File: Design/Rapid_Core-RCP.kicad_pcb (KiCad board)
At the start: 4 copper layers, 222 parts, among them IC1 TLIN1039DDFRQ1, IC2 TLIN1039DDFRQ1, IC3 SHT30A-DIS-B2.5KS, IC4 LM60440ARPKR, J1 CMD PIN, J10 CAN-1, J11 RS-485_1, J12 RS-485_2, J14 CAN-2, J15 Input Power, J2 CMD PIN, J3 LIN_1, J4 LIN_2, J5 GPIO_CONN_x_4, J6 SWD_Debug, J7 SPI_CONN, J8 USART, SW1 SW_Push, U1 STM32F446RETx, U2 ISO1042BQDWVRQ1, U3 ISO3082DW, U4 ISO3082DW, U5 ISO1042BQDWVRQ1, U6 CRE1S0505S3C, U7 CRE1S0505S3C, U8 LP3963-3.3, Y1 8_MHz, Y2 32.768_KHz

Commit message: PCB design started, comps arranged
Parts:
- removed FB1: FerriteBead, Inductor_SMD:L_0805_2012Metric_Pad1.05x1.20mm_HandSolder
- removed R11, R12, R13, R14: 0, Resistor_SMD:R_0603_1608Metric_Pad0.98x0.95mm_HandSolder
- J7: value SPI_CONN -> SPI; footprint Connector_PinHeader_2.54mm:PinHeader_1x10_P2.54mm_Vertical -> Connector_PinHeader_2.54mm:PinHeader_1x05_P2.54mm_Vertical
- L1, L2, L3: value 51uH 0.2A 1R -> ACT45B-510-2P-TL003
- L4: value 51u 0.2A 1R -> ACT45B-510-2P-TL003
- TP1, TP10, TP11, TP12, TP13, TP14, TP15, TP16, TP17, TP18, TP19, TP2, TP20, TP21, TP22, TP23, TP24, TP25, TP26, TP27, TP28, TP29, TP3, TP30, TP31, TP32, TP33, TP34, TP35, TP36, TP37, TP38, TP39, TP4, TP40, TP41, TP42, TP43, TP44, TP45, TP46, TP47, TP48, TP49, TP5, TP50, TP51, TP52, TP53, TP54, TP55, TP56, TP57, TP58, TP59, TP6, TP60, TP61, TP62, TP7, TP8, TP9: footprint TestPoint:TestPoint_Pad_D2.5mm -> TestPoint:TestPoint_Pad_D1.0mm
- moved TP10 218.4 mm to (-42.5, 142.7)
- moved TP3 218.4 mm to (-47.1, 133.6)
- moved TP4 218.4 mm to (-47.1, 138.1)
- moved TP5 218.4 mm to (-47.1, 142.7)
- moved TP6 218.4 mm to (-42.5, 124.5)
- moved TP7 218.4 mm to (-42.5, 129.0)
- moved TP8 218.4 mm to (-42.5, 133.6)
- moved TP9 218.4 mm to (-42.5, 138.1)
- moved C62 218.4 mm to (-66.9, 87.7)
- moved TP11 218.4 mm to (-38.0, 124.5)
- moved TP12 218.4 mm to (-38.0, 129.0)
- moved TP13 218.4 mm to (-38.0, 133.6)
- moved TP14 218.4 mm to (-38.0, 138.1)
- moved TP45 215.6 mm to (305.0, 155.4)
- moved TP46 215.6 mm to (305.0, 160.0)
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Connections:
- net /Communication_interface/CAN1_RX_R renamed /Communication_interface/CAN1_RX_R-1
- net /Communication_interface/CAN1_TX_R renamed /Communication_interface/CAN1_TX_R-1
- net /Communication_interface/CAN2_RX_R renamed /Communication_interface/CAN2_RX_R-2
- net /Communication_interface/CAN2_TX_R renamed /Communication_interface/CAN2_TX_R-2
- net /Communication_interface/RS-485_1_EN_R renamed /Communication_interface/RS-485_1_EN_R-1
- net /Communication_interface/RS-485_1_RX_R renamed /Communication_interface/RS-485_1_RX_R-1
- net /Communication_interface/RS-485_1_TX_R renamed /Communication_interface/RS-485_1_TX_R-1
- net /Communication_interface/RS-485_2_EN_R renamed /Communication_interface/RS-485_2_EN_R-2
- net /Communication_interface/RS-485_2_RX_R renamed /Communication_interface/RS-485_2_RX_R-2
- net /Communication_interface/RS-485_2_TX_R renamed /Communication_interface/RS-485_2_TX_R-2
- C15 pad 1: /FIL_FB -> +3.3V
- C18 pad 1: /FIL_FB -> +3.3V
- D5 pad 1: /Communication_interface/CAN_H -> /Communication_interface/CAN_H_IN-1
- D5 pad 2: /Communication_interface/CAN_L -> /Communication_interface/CAN_L_IN-1
- D6 pad 1: /Communication_interface/RS-485_B -> /Communication_interface/RS-485_B_IN-2
- D6 pad 2: /Communication_interface/RS-485_A -> /Communication_interface/RS-485_A_IN-2
- D7 pad 1: /Communication_interface/RS-485_B -> /Communication_interface/RS-485_B_IN-1
- D7 pad 2: /Communication_interface/RS-485_A -> /Communication_interface/RS-485_A-IN-1
- D8 pad 1: /Communication_interface/CAN_H -> /Communication_interface/CAN_H_IN-2
- D8 pad 2: /Communication_interface/CAN_L -> /Communication_interface/CAN_L_IN-2
- J10 pad 1: /Communication_interface/CAN_H -> /Communication_interface/CAN_L_IN-1
- J10 pad 2: /Communication_interface/CAN_L -> /Communication_interface/CAN_H_IN-1
- J11 pad 1: /Communication_interface/RS-485_B -> /Communication_interface/RS-485_A-IN-1
- J11 pad 2: /Communication_interface/RS-485_A -> /Communication_interface/RS-485_B_IN-1
- J12 pad 1: /Communication_interface/RS-485_B -> /Communication_interface/RS-485_A_IN-2
- J12 pad 2: /Communication_interface/RS-485_A -> /Communication_interface/RS-485_B_IN-2
- J14 pad 1: /Communication_interface/CAN_H -> /Communication_interface/CAN_L_IN-2
- J14 pad 2: /Communication_interface/CAN_L -> /Communication_interface/CAN_H_IN-2
- J15 pad 1: GND1 -> +24V
- J15 pad 2: +24V -> GND1
- L1 pad 1: /Communication_interface/CAN_H -> /Communication_interface/CAN_H-1
- L1 pad 2: /Communication_interface/CAN_H -> /Communication_interface/CAN_L-1
- L1 pad 3: /Communication_interface/CAN_L -> /Communication_interface/CAN_L_IN-1
- L1 pad 4: /Communication_interface/CAN_L -> /Communication_interface/CAN_H_IN-1
- L2 pad 1: /Communication_interface/RS-485_B -> /Communication_interface/RS-485_B-1
- L2 pad 2: /Communication_interface/RS-485_B -> /Communication_interface/RS-485_A-1
- L2 pad 3: /Communication_interface/RS-485_A -> /Communication_interface/RS-485_A-IN-1
- L2 pad 4: /Communication_interface/RS-485_A -> /Communication_interface/RS-485_B_IN-1
- L3 pad 1: /Communication_interface/RS-485_B -> /Communication_interface/RS-485_B-2
- L3 pad 2: /Communication_interface/RS-485_B -> /Communication_interface/RS-485_A-2
- L3 pad 3: /Communication_interface/RS-485_A -> /Communication_interface/RS-485_A_IN-2
- L3 pad 4: /Communication_interface/RS-485_A -> /Communication_interface/RS-485_B_IN-2
- L4 pad 1: /Communication_interface/CAN_H -> /Communication_interface/CAN_H-2
- L4 pad 2: /Communication_interface/CAN_H -> /Communication_interface/CAN_L-2
- L4 pad 3: /Communication_interface/CAN_L -> /Communication_interface/CAN_L_IN-2
- L4 pad 4: /Communication_interface/CAN_L -> /Communication_interface/CAN_H_IN-2
- R23 pad 1: /Communication_interface/CAN_H -> /Communication_interface/CAN_H-1
- R23 pad 2: /Communication_interface/CAN_H -> /Communication_interface/CAN_H_IN-1
- R24 pad 1: /Communication_interface/CAN_L -> /Communication_interface/CAN_L-1
- R24 pad 2: /Communication_interface/CAN_L -> /Communication_interface/CAN_L_IN-1
- R25 pad 1: /Communication_interface/RS-485_B -> /Communication_interface/RS-485_B-1
- R25 pad 2: /Communication_interface/RS-485_B -> /Communication_interface/RS-485_B_IN-1
- R26 pad 1: /Communication_interface/RS-485_A -> /Communication_interface/RS-485_A-1
- R26 pad 2: /Communication_interface/RS-485_A -> /Communication_interface/RS-485_A-IN-1
- R27 pad 1: /Communication_interface/CAN_H -> /Communication_interface/CAN_H_IN-1
- R27 pad 2: /Communication_interface/CAN_L -> /Communication_interface/CAN_L_IN-1
- R28 pad 1: /Communication_interface/RS-485_A -> /Communication_interface/RS-485_A-2
- R28 pad 2: /Communication_interface/RS-485_A -> /Communication_interface/RS-485_A_IN-2
- R29 pad 1: /Communication_interface/RS-485_B -> /Communication_interface/RS-485_B-2
- R29 pad 2: /Communication_interface/RS-485_B -> /Communication_interface/RS-485_B_IN-2
- R30 pad 1: /Communication_interface/RS-485_B -> /Communication_interface/RS-485_B-2
- R31 pad 1: /Communication_interface/RS-485_A -> /Communication_interface/RS-485_A-2
- R32 pad 1: /Communication_interface/RS-485_B -> /Communication_interface/RS-485_B-1
- R33 pad 1: /Communication_interface/RS-485_A -> /Communication_interface/RS-485_A-1
- R34 pad 1: /Communication_interface/RS-485_B -> /Communication_interface/RS-485_B_IN-2
- R34 pad 2: /Communication_interface/RS-485_A -> /Communication_interface/RS-485_A_IN-2
- R35 pad 1: /Communication_interface/RS-485_B -> /Communication_interface/RS-485_B_IN-1
- R35 pad 2: /Communication_interface/RS-485_A -> /Communication_interface/RS-485_A-IN-1
- R38 pad 1: /Communication_interface/CAN_H -> /Communication_interface/CAN_H-2
- R38 pad 2: /Communication_interface/CAN_H -> /Communication_interface/CAN_H_IN-2
- R39 pad 1: /Communication_interface/CAN_L -> /Communication_interface/CAN_L-2
- R39 pad 2: /Communication_interface/CAN_L -> /Communication_interface/CAN_L_IN-2
- R40 pad 1: /Communication_interface/CAN_H -> /Communication_interface/CAN_H_IN-2
- R40 pad 2: /Communication_interface/CAN_L -> /Communication_interface/CAN_L_IN-2
- R47 pad 1: /Communication_interface/CAN_H -> /Communication_interface/CAN_H_IN-1
- R48 pad 2: /Communication_interface/CAN_L -> /Communication_interface/CAN_L_IN-1
- TP43 pad 1: /Communication_interface/CAN_H -> /Communication_interface/CAN_H_IN-1
- TP44 pad 1: /Communication_interface/CAN_L -> /Communication_interface/CAN_L_IN-1
- TP45 pad 1: /Communication_interface/RS-485_A -> /Communication_interface/RS-485_A_IN-2
- TP46 pad 1: /Communication_interface/RS-485_B -> /Communication_interface/RS-485_B_IN-2
- TP47 pad 1: /Communication_interface/RS-485_B -> /Communication_interface/RS-485_B_IN-1
- TP48 pad 1: /Communication_interface/RS-485_A -> /Communication_interface/RS-485_A-IN-1
- TP51 pad 1: /Communication_interface/CAN_H -> /Communication_interface/CAN_H_IN-2
- TP52 pad 1: /Communication_interface/CAN_L -> /Communication_interface/CAN_L_IN-2
- U1 pad 10: /SPI2_MISO -> unconnected-(U1-PC2-Pad10)
- U1 pad 9: /SPI2_MOSI -> unconnected-(U1-PC1-Pad9)
- U2 pad 6: /Communication_interface/CAN_L -> /Communication_interface/CAN_L-1
- U2 pad 7: /Communication_interface/CAN_H -> /Communication_interface/CAN_H-1
- U3 pad 12: /Communication_interface/RS-485_A -> /Communication_interface/RS-485_A-1
- U3 pad 13: /Communication_interface/RS-485_B -> /Communication_interface/RS-485_B-1
- U4 pad 12: /Communication_interface/RS-485_A -> /Communication_interface/RS-485_A-2
- U4 pad 13: /Communication_interface/RS-485_B -> /Communication_interface/RS-485_B-2
- U5 pad 6: /Communication_interface/CAN_L -> /Communication_interface/CAN_L-2
- U5 pad 7: /Communication_interface/CAN_H -> /Communication_interface/CAN_H-2
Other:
- board outline added: 151.1 x 100.3 mm

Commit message: Temp complete of communication section , added Safety caps
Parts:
- removed C62: 4700pF, Capacitor_SMD:C_0603_1608Metric_Pad1.08x0.95mm_HandSolder
- removed R47, R48: 59, Resistor_SMD:R_0603_1608Metric_Pad0.98x0.95mm_HandSolder
- removed TP10, TP11, TP12, TP13, TP14, TP15, TP16, TP17, TP18, TP19, TP20, TP21, TP22, TP23, TP24, TP25, TP26, TP27, TP28, TP29, TP3, TP30, TP31, TP32, TP33, TP34, TP35, TP36, TP37, TP38, TP39, TP4, TP40, TP41, TP42, TP43, TP44, TP45, TP46, TP47, TP48, TP49, TP5, TP50, TP51, TP52, TP53, TP54, TP55, TP56, TP57, TP58, TP59, TP6, TP60, TP61, TP62, TP7, TP8, TP9: TestPoint, TestPoint:TestPoint_Pad_D1.0mm
- R15, R16, R17, R18, R19, R20, R21, R22, R23, R24, R25, R26, R28, R29, R36, R37, R38, R39: footprint Resistor_SMD:R_0603_1608Metric_Pad0.98x0.95mm_HandSolder -> Resistor_SMD:R_0805_2012Metric_Pad1.20x1.40mm_HandSolder
- R27, R34, R35, R40: footprint Resistor_SMD:R_0805_2012Metric_Pad1.20x1.40mm_HandSolder -> Resistor_SMD:R_2512_6332Metric_Pad1.40x3.35mm_HandSolder
- Y1: value 8_MHz -> Crystal_GND24; footprint ECS-2520MVLC_8MHz:ECS2520MVLC080BNTR -> Crystal:Crystal_SMD_2520-4Pin_2.5x2.0mm
- moved H3 126.5 mm to (213.6, 52.8)
- moved H4 94.5 mm to (213.4, 121.7)
- moved H1 88.8 mm to (76.5, 51.8)
- moved C16 78.1 mm to (121.7, 88.9), turned to 180 degrees
- moved C2 69.0 mm to (103.5, 79.7)
- moved C1 69.0 mm to (103.7, 77.9)
- moved R3 69.0 mm to (108.8, 84.0)
- moved R4 69.0 mm to (108.8, 81.0)
- moved IC3 69.0 mm to (104.0, 82.3)
- moved R20 67.8 mm to (154.1, 101.6)
- moved R22 67.7 mm to (154.1, 99.3)
- moved C31 67.6 mm to (158.2, 93.7)
- moved R21 67.5 mm to (154.1, 97.3)
- moved C29 67.3 mm to (160.3, 94.0)
- moved C27 67.0 mm to (162.1, 94.0)
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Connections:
- H3 pad 1: GND1 -> GND2
- H4 pad 1: GND1 -> GND2
- U1 pad 1: GND1 -> +3.3V
- U1 pad 29: /SPI2_SCK -> unconnected-(U1-PB10-Pad29)
- Y1 pad 1: GND1 -> /HSE_OUT
- Y1 pad 2: /HSE_IN -> GND1
- Y1 pad 3: /HSE_OUT -> /HSE_IN
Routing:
- net GND1: track 0.00 -> 79.4 mm, vias 0 -> 28
- net GND2: track 0.00 -> 63.8 mm, vias 0 -> 112
- net CAN1_TX: track 0.00 -> 38.4 mm
- net CAN1_RX: track 0.00 -> 38.1 mm
- net RS-485_1_RX: track 0.00 -> 27.6 mm
- net /Communication_interface/CAN_L_IN-2: track 0.00 -> 26.0 mm
- net /Communication_interface/CAN_H_IN-2: track 0.00 -> 25.1 mm
- net RS-485_1_EN: track 0.00 -> 24.7 mm, vias 0 -> 2
- net /Communication_interface/RS-485_A_IN-2: track 0.00 -> 24.6 mm
- net /Communication_interface/CAN_L_IN-1: track 0.00 -> 24.4 mm
- net /Communication_interface/CAN_H_IN-1: track 0.00 -> 24.0 mm
- net /Communication_interface/RS-485_B_IN-2: track 0.00 -> 24.0 mm
- net /Communication_interface/RS-485_A-IN-1: track 0.00 -> 23.5 mm
- net /Communication_interface/RS-485_B_IN-1: track 0.00 -> 23.3 mm
- net /HSE_OUT: track 0.00 -> 22.9 mm
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- added copper zone on F.Cu, net +3.3V
- added copper zone on B.Cu, net +5VA
- added copper zone on F.Cu, net +5VA
- added copper zone on F.Cu, net GND1
- added copper zone on In1.Cu, net GND2
- added copper zone on In2.Cu, net GND2
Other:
- board size 151.1 x 100.3 mm -> 144.3 x 77.7 mm
- rule pad_to_mask_clearance: 0 -> 0.08
- board text added: "Isolation _1"
- board text added: "Isolation _2"

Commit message: Added all the sections
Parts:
- removed FID4: Fiducial, Fiducial:Fiducial_1.5mm_Mask3mm
- R3, R4: value 10K -> 4k7
- moved FID3 131.4 mm to (205.7, 57.1)
- moved FID2 59.3 mm to (83.1, 53.3)
- moved C60 27.7 mm to (97.8, 56.6)
- moved R7 26.7 mm to (95.9, 84.8)
- moved D3 26.7 mm to (91.6, 84.8)
- moved C58 23.8 mm to (97.6, 58.9), turned to 0 degrees
- moved C59 23.7 mm to (93.5, 58.9), turned to 180 degrees
- moved R8 21.2 mm to (95.9, 82.3)
- moved D4 21.1 mm to (91.6, 82.3)
- moved L5 13.7 mm to (95.6, 63.8), turned to 90 degrees
- moved R41 13.3 mm to (84.9, 103.9)
- moved C57 11.9 mm to (100.9, 75.6)
- moved D2 11.2 mm to (122.7, 58.4)
- moved R46 11.2 mm to (97.3, 75.2), turned to 90 degrees
- moved R44 11.1 mm to (101.9, 71.3), turned to 0 degrees
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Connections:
- net /Power_Stage/LM_SW_1 renamed /Power_Stage/LM_SW
- C53 pad 1: /Power_Stage/LM_VCC1 -> /Power_Stage/LM_VCC
- C54 pad 1: /Power_Stage/LM_VCC2 -> /Power_Stage/LM_VCC
- IC4 pad 15: /Power_Stage/LM_VCC2 -> /Power_Stage/LM_VCC
- IC4 pad 5: /Power_Stage/LM_VCC1 -> /Power_Stage/LM_VCC
- J6 pad 2: /NRST -> /SW_CLK
- J6 pad 3: /SW_CLK -> /NRST
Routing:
- net /NRST: track 12.5 -> 89.5 mm, vias 0 -> 2
- net /SWDIO: track 3.76 -> 48.1 mm
- net /SW_CLK: track 0.00 -> 42.4 mm
- net /USR_LED_1: track 0.00 -> 41.3 mm, vias 0 -> 2
- net /USR_LED_2: track 0.00 -> 37.5 mm, vias 0 -> 2
- net /LIN2_RX: track 0.00 -> 32.0 mm
- net /LIN2_EN: track 0.00 -> 31.8 mm, vias 0 -> 2
- net CAN2_RX: track 0.00 -> 30.8 mm
- net CAN2_TX: track 0.00 -> 29.9 mm
- net /LIN2_TX: track 0.00 -> 28.8 mm
- net /USART2_TX: track 0.00 -> 27.4 mm
- net /LIN1_EN: track 0.00 -> 25.3 mm, vias 0 -> 2
- net /USART2_RX: track 0.00 -> 24.4 mm
- net /LIN1_TX: track 0.00 -> 21.7 mm
- net /SPI1_SCK: track 0.00 -> 21.5 mm
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- added copper zone on B.Cu, net +24V
- added copper zone on F.Cu, net +24V
- added copper zone on B.Cu, net +3.3V
- added copper zone on F.Cu, net +5V
- added copper zone on F.Cu, net /Power_Stage/LM_VCC
- added copper zone on In1.Cu, net GND1
- added copper zone on In2.Cu, net GND1
- removed copper zone on B.Cu, net +5VA
- removed copper zone on In1.Cu, net GND2
- removed copper zone on In2.Cu, net GND2
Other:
- rule solder_mask_min_width: 0.125 -> 0.1

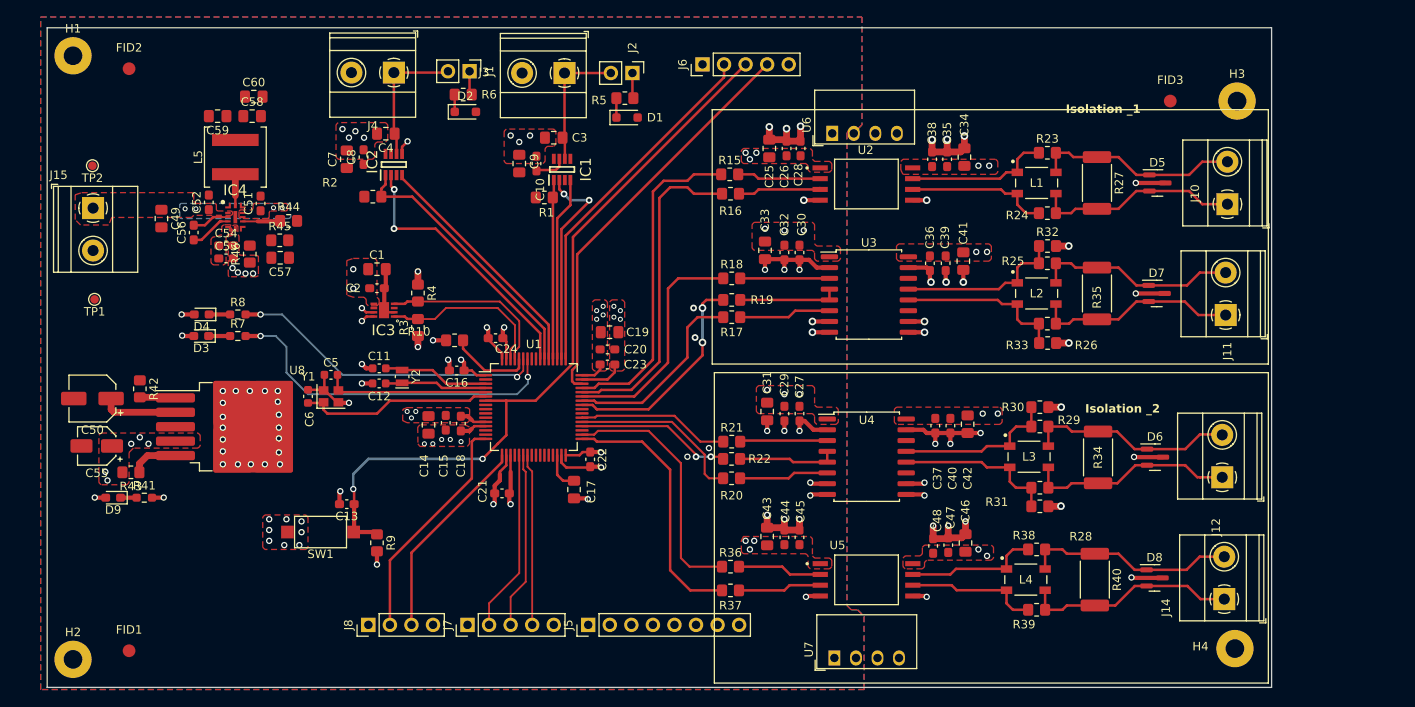
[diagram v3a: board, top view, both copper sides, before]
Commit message: Added lib folder, Layer layed
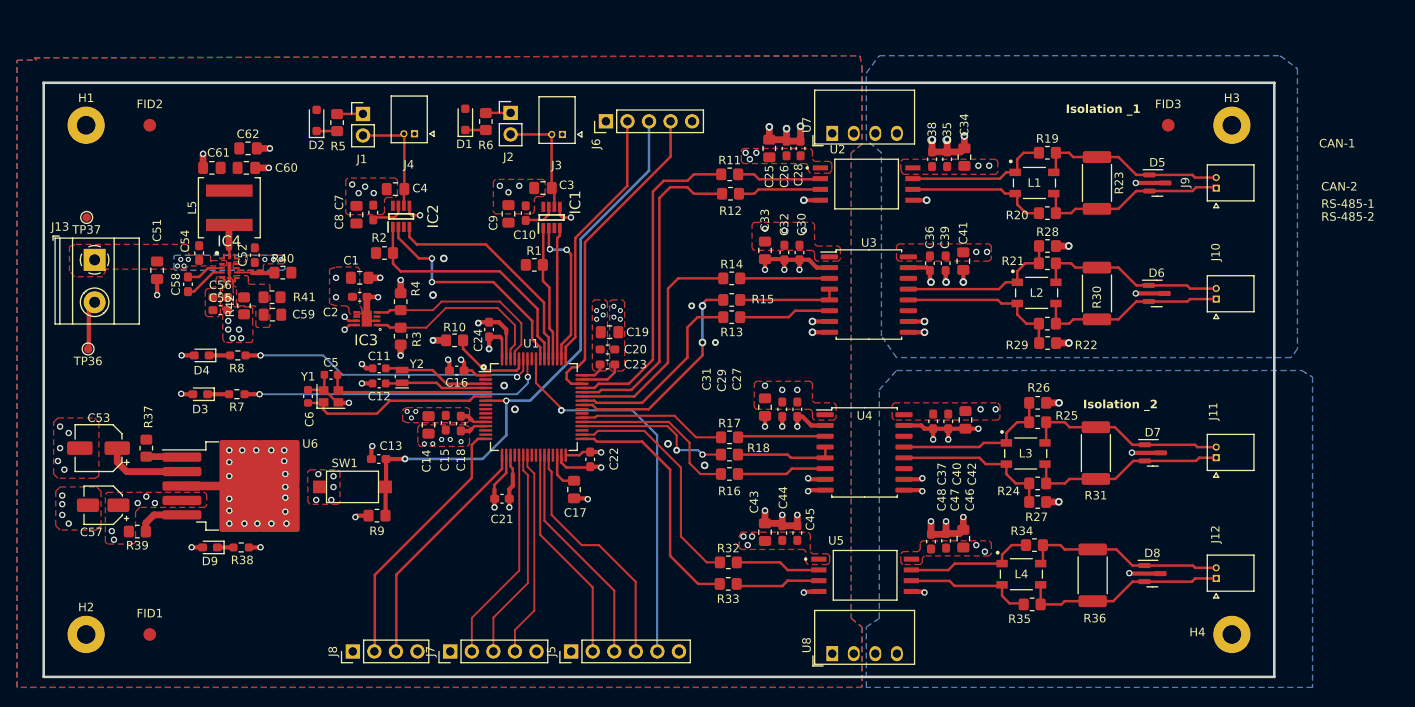
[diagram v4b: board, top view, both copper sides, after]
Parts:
- removed J14: CAN-2, TerminalBlock_Phoenix:TerminalBlock_Phoenix_MKDS-1,5-2_1x02_P5.00mm_Horizontal
- added J9: CAN-1, 0530480210_2pin_P1.25_PicoBlade:MOLEX_530480210, F.Cu at (211.2, 67.4)
- J1: value CMD PIN -> LIN-2
- J10: value CAN-1 -> RS-485-1; footprint TerminalBlock_Phoenix:TerminalBlock_Phoenix_MKDS-1,5-2_1x02_P5.00mm_Horizontal -> 0530480210_2pin_P1.25_PicoBlade:MOLEX_530480210
- J11: value RS-485_1 -> RS-485-2; footprint TerminalBlock_Phoenix:TerminalBlock_Phoenix_MKDS-1,5-2_1x02_P5.00mm_Horizontal -> 0530480210_2pin_P1.25_PicoBlade:MOLEX_530480210
- J12: value RS-485_2 -> CAN-2; footprint TerminalBlock_Phoenix:TerminalBlock_Phoenix_MKDS-1,5-2_1x02_P5.00mm_Horizontal -> 0530480210_2pin_P1.25_PicoBlade:MOLEX_530480210
- J2: value CMD PIN -> LIN-1
- J3: value LIN_1 -> LIN-1; footprint TerminalBlock_Phoenix:TerminalBlock_Phoenix_MKDS-1,5-2_1x02_P5.00mm_Horizontal -> 0530480210_2pin_P1.25_PicoBlade:MOLEX_530480210
- J4: value LIN_2 -> LIN-2; footprint TerminalBlock_Phoenix:TerminalBlock_Phoenix_MKDS-1,5-2_1x02_P5.00mm_Horizontal -> 0530480210_2pin_P1.25_PicoBlade:MOLEX_530480210
- J5: value GPIO_CONN_x_4 -> GPIO_CONN_X_4; footprint Connector_PinHeader_2.54mm:PinHeader_1x08_P2.54mm_Vertical -> Connector_PinHeader_2.54mm:PinHeader_1x06_P2.54mm_Vertical
- moved D1 19.1 mm to (122.7, 59.3), turned to 90 degrees
- moved D2 17.6 mm to (105.2, 59.4), turned to 90 degrees
- moved J11 16.9 mm to (211.2, 99.2)
- moved R6 16.6 mm to (125.1, 59.6), turned to -90 degrees
- moved R5 15.2 mm to (107.6, 59.7), turned to -90 degrees
- moved J2 15.1 mm to (128.0, 58.5), turned to 0 degrees
- moved J1 13.5 mm to (110.6, 58.7), turned to 0 degrees
- moved J6 13.2 mm to (139.2, 59.5)
- moved D9 12.8 mm to (92.6, 109.7)
- moved R38 12.8 mm to (96.3, 109.7)
- moved J12 11.9 mm to (211.2, 113.4)
- moved J10 11.3 mm to (211.2, 80.5)
- moved H1 8.33 mm to (78.0, 60.0)
- moved R1 8.03 mm to (130.8, 76.5)
- moved J4 7.61 mm to (116.7, 61.0)
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- renumbered C49 to C51, C51 to C52, C50 to C53, C52 to C54, C53 to C55, C54 to C56, C55 to C57, C56 to C58, C57 to C59, C58 to C60, C59 to C61, C60 to C62, D7 to D6, D6 to D7, J15 to J13, R15 to R11, R16 to R12, R17 to R13, R18 to R14, R19 to R15, R20 to R16, R21 to R17, R22 to R18, R23 to R19, R24 to R20, R25 to R21, R26 to R22, R27 to R23, R28 to R24, R29 to R25, R30 to R26, R31 to R27, R32 to R28, R33 to R29, R35 to R30, R34 to R31, R36 to R32, R37 to R33, R38 to R34, R39 to R35, R40 to R36, R42 to R37, R41 to R38, R43 to R39, R44 to R40, R45 to R41, R46 to R42, R6 to R5, R5 to R6, TP1 to TP36, TP2 to TP37, U8 to U6, U6 to U7, U7 to U8
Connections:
- J10 pad 1: /Communication_interface/CAN_L_IN-1 -> /Communication_interface/RS-485_A-IN-1
- J10 pad 2: /Communication_interface/CAN_H_IN-1 -> /Communication_interface/RS-485_B_IN-1
- J11 pad 1: /Communication_interface/RS-485_A-IN-1 -> /Communication_interface/RS-485_A_IN-2
- J11 pad 2: /Communication_interface/RS-485_B_IN-1 -> /Communication_interface/RS-485_B_IN-2
- J12 pad 1: /Communication_interface/RS-485_A_IN-2 -> /Communication_interface/CAN_L_IN-2
- J12 pad 2: /Communication_interface/RS-485_B_IN-2 -> /Communication_interface/CAN_H_IN-2
- J3 pad 1: /LIN1 -> GND1
- J3 pad 2: GND1 -> /LIN1
- J4 pad 1: /LIN2 -> GND1
- J4 pad 2: GND1 -> /LIN2
- J5 pad 4: GND1 -> /GPIO_1_PB2
- J5 pad 5: /GPIO_1_PB2 -> /GPIO_1_PB3
- J5 pad 6: /GPIO_1_PB4 -> GND1
- U1 pad 56: /GPIO_1_PB4 -> /GPIO_1_PB3
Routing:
- net /GPIO_1_PB3: track 0.00 -> 45.3 mm, vias 0 -> 1
- net GND1: track 100.7 -> 130.2 mm, vias 82 -> 99
- net /GPIO_1_PB2: track 0.00 -> 28.6 mm
- net /GPIO_1_PB1: track 0.00 -> 26.5 mm
- net /GPIO_1_PB0: track 0.00 -> 25.7 mm
- net /NRST: track 89.5 -> 70.1 mm
- net /SW_CLK: track 42.4 -> 31.0 mm
- net /SWDIO: track 48.1 -> 37.9 mm
- net /LIN1_EN: track 25.3 -> 18.1 mm
- net /LIN1_TX: track 21.7 -> 15.5 mm
- net /LIN1_RX: track 21.1 -> 15.4 mm
- net +5V: track 13.1 -> 17.8 mm
- net /USR_LED_1: track 41.3 -> 36.8 mm
- net /LIN2_EN: track 31.8 -> 27.6 mm
- net /SPI1_MOSI: track 20.2 -> 24.4 mm
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- added copper zone on B.Cu, net +5VA
- added copper zone on F.Cu, net /Power_Stage/LM_FB
- added copper zone on In1.Cu, net GND2
- added copper zone on In2.Cu, net GND2
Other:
- board size 144.3 x 77.7 mm -> 145 x 70 mm
- board text added: "CAN-1"
- board text added: "CAN-2"
- board text added: "RS-485-1"
- board text added: "RS-485-2"

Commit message: End of version 1.0.0 design
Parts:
- removed TP36, TP37: TestPoint, TestPoint:TestPoint_Pad_D1.0mm
- SW1: footprint Button_Switch_SMD:SW_SPST_CK_RS282G05A3 -> Button_Switch_SMD:SW_Tactile_SPST_NO_Straight_CK_PTS636Sx25SMTRLFS
- moved J6 9.27 mm to (137.2, 68.6)
- moved R8 8.28 mm to (93.7, 95.1)
- moved D4 8.27 mm to (89.5, 95.1)
- moved C1 7.15 mm to (108.2, 84.8)
- moved C14 7.15 mm to (116.3, 102.2)
- moved C18 7.15 mm to (120.1, 102.0)
- moved C2 7.15 mm to (108.2, 87.1)
- moved C20 7.15 mm to (137.4, 93.3)
- moved C23 7.15 mm to (137.4, 95.1)
- moved C25 7.15 mm to (156.5, 69.6)
- moved C27 7.15 mm to (159.8, 100.3)
- moved C28 7.15 mm to (160.1, 69.6)
- moved C29 7.15 mm to (158.0, 100.3)
- moved C32 7.15 mm to (158.2, 81.9)
- moved C37 7.15 mm to (175.8, 101.8)
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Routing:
- net GND1: track 130.2 -> 124.6 mm, vias 99 -> 101
- net /GPIO_1_PB2: track 28.6 -> 25.2 mm
- net /GPIO_1_PB0: track 25.7 -> 22.3 mm
- net /GPIO_1_PB3: track 45.3 -> 41.9 mm
- net /SPI1_SCK: track 25.4 -> 22.1 mm
- net /SPI1_MISO: track 25.0 -> 21.6 mm
- net /SPI1_MOSI: track 24.4 -> 21.0 mm
- net /GPIO_1_PB1: track 26.5 -> 23.2 mm
- net /USART2_RX: track 28.3 -> 24.9 mm
- net /USART2_TX: track 31.0 -> 27.6 mm
- net /NRST: track 70.1 -> 67.9 mm
- net /SWDIO: track 37.9 -> 35.7 mm
- net /SW_CLK: track 31.0 -> 28.8 mm
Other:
- outline, holes or cut-outs redrawn
- rule pad_to_mask_clearance: 0.08 -> 0.05
- board text added: "+"
- board text added: "3.3V"
- board text added: "A"
- board text added: "B"
- board text added: "CAN-H"
- board text added: "CAN-L"
- board text added: "CLK"
- board text added: "DIO"
- board text added: "GND"
- board text added: "GPIO"
- board text added: "J10"
- board text added: "J11"
- board text added: "J12"
- board text added: "J3"
- board text added: "J4"
- board text added: "J9"
- board text added: "LIN"
- board text added: "MISO"
- board text added: "MOSI"
- board text added: "NRST"
- board text added: "NRST_SW"
- board text added: "PB0"
- board text added: "PB1"
- board text added: "PB2"
- board text added: "PB3"
- board text added: "PWR_LED"
- board text added: "RX"
- board text added: "SCK"
- board text added: "SPI"
- board text added: "SWD"
- board text added: "TX"
- board text added: "U2"
- board text added: "U5"
- board text added: "UART"
- board text added: "USR_1"
- board text added: "USR_2"
- board text removed: "Isolation _1"
- board text removed: "Isolation _2"

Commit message: Added everything
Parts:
- added G2: Not_to_bin, Not_To_Bin:Not_To_Bin, F.Cu at (90.8, 125.4)
- added G3: NOON_REAY_ENERGIES, Noon_Ray:Noon_Ray, F.Cu at (99.2, 124.6)
- added G4: High_Voltage_Warning, High_Voltage_Warning_logo:High_Voltage_Warning, F.Cu at (83.4, 74.1)
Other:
- outline, holes or cut-outs redrawn
